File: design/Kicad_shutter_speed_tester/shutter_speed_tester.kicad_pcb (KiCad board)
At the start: 2 copper layers, 17 parts, among them J1 Light Sensor, J2 Light source LED, J3 LCD, J4 Power, Q1 PN2222A, SW1 Reset switch

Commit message: adding routing
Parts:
- moved H4 2.84 mm to (213.4, 129.5)
- moved H3 2.84 mm to (170.2, 129.5)
- moved H2 2.54 mm to (213.4, 85.1)
- moved J3 2.54 mm to (172.7, 119.4)
- moved H1 2.54 mm to (170.2, 85.1)
- moved J4 1.27 mm to (179.1, 110.5)
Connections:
- J4 pad 1: Net-(A1-Pad30) -> GND
- J4 pad 2: GND -> Net-(A1-Pad30)
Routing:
- net GND: track 0.00 -> 87.2 mm
- net Net-(A1-Pad5): track 0.00 -> 63.2 mm
- net Net-(J2-Pad1): track 0.00 -> 57.3 mm
- net Net-(A1-Pad27): track 0.00 -> 52.0 mm
- net Net-(A1-Pad7): track 0.00 -> 43.0 mm
- net Net-(A1-Pad30): track 0.00 -> 31.6 mm
- net Net-(D1-Pad1): track 0.00 -> 29.1 mm
- net Net-(Q1-Pad2): track 0.00 -> 22.6 mm
- net Net-(A1-Pad6): track 0.00 -> 19.1 mm
- net Net-(A1-Pad23): track 0.00 -> 14.6 mm
- net Net-(A1-Pad8): track 0.00 -> 12.5 mm
- net Net-(Q1-Pad3): track 0.00 -> 12.0 mm
- net Net-(A1-Pad24): track 0.00 -> 11.0 mm
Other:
- board outline added: 50.8 x 52.1 mm
- board text added: "LCD"
- board text added: "Light Sensor"
- board text added: "Light Source"
- board text added: "Power"

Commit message: pcb design described
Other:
- board text added: "+"
- board text added: "+5V"
- board text added: "-"
- board text added: "Gnd"
- board text added: "SCL"
- board text added: "SDA"
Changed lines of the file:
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@@
   (general
     (thickness 1.6)
-    (drawings 8)
+    (drawings 22)
     (tracks 77)
     (zones 0)
@@
     )
   )
+  (gr_text SCL (at 180.34 124.46 90) (layer F.SilkS)
+    (effects (font (size 1 1) (thickness 0.15)))
+  )
+  (gr_text SDA (at 177.8 124.46 90) (layer F.SilkS)
+    (effects (font (size 1 1) (thickness 0.15)))
+  )
+  (gr_text +5V (at 175.26 124.46 90) (layer F.SilkS)
+    (effects (font (size 1 1) (thickness 0.15)))
+  )
+  (gr_text Gnd (at 172.72 124.46 90) (layer F.SilkS)
+    (effects (font (size 1 1) (thickness 0.15)))
+  )
+  (gr_text + (at 176.53 114.3) (layer F.SilkS)
+    (effects (font (size 1 1) (thickness 0.15)))
+  )
+  (gr_text - (at 179.07 114.3) (layer F.SilkS)
+    (effects (font (size 1 1) (thickness 0.15)))
+  )
+  (gr_text - (at 179.07 105.41) (layer F.SilkS)
+    (effects (font (size 1 1) (thickness 0.15)))
+  )
+  (gr_text + (at 176.53 105.41) (layer F.SilkS)
+    (effects (font (size 1 1) (thickness 0.15)))
+  )
+  (gr_text - (at 179.07 96.52) (layer F.SilkS)
+    (effects (font (size 1 1) (thickness 0.15)))
+  )
+  (gr_text + (at 176.53 96.52) (layer F.SilkS)
+    (effects (font (size 1 1) (thickness 0.15)))
+  )
+  (gr_line (start 196.85 83.82) (end 189.23 83.82) (layer F.SilkS) (width 0.12))
+  (gr_line (start 196.85 93.98) (end 196.85 83.82) (layer F.SilkS) (width 0.12))
+  (gr_line (start 189.23 93.98) (end 196.85 93.98) (layer F.SilkS) (width 0.12))
+  (gr_line (start 189.23 83.82) (end 189.23 93.98) (layer F.SilkS) (width 0.12))
   (gr_line (start 217.17 81.28) (end 217.17 133.35) (layer Edge.Cuts) (width 0.1))
   (gr_line (start 166.37 81.28) (end 217.17 81.28) (layer Edge.Cuts) (width 0.1))

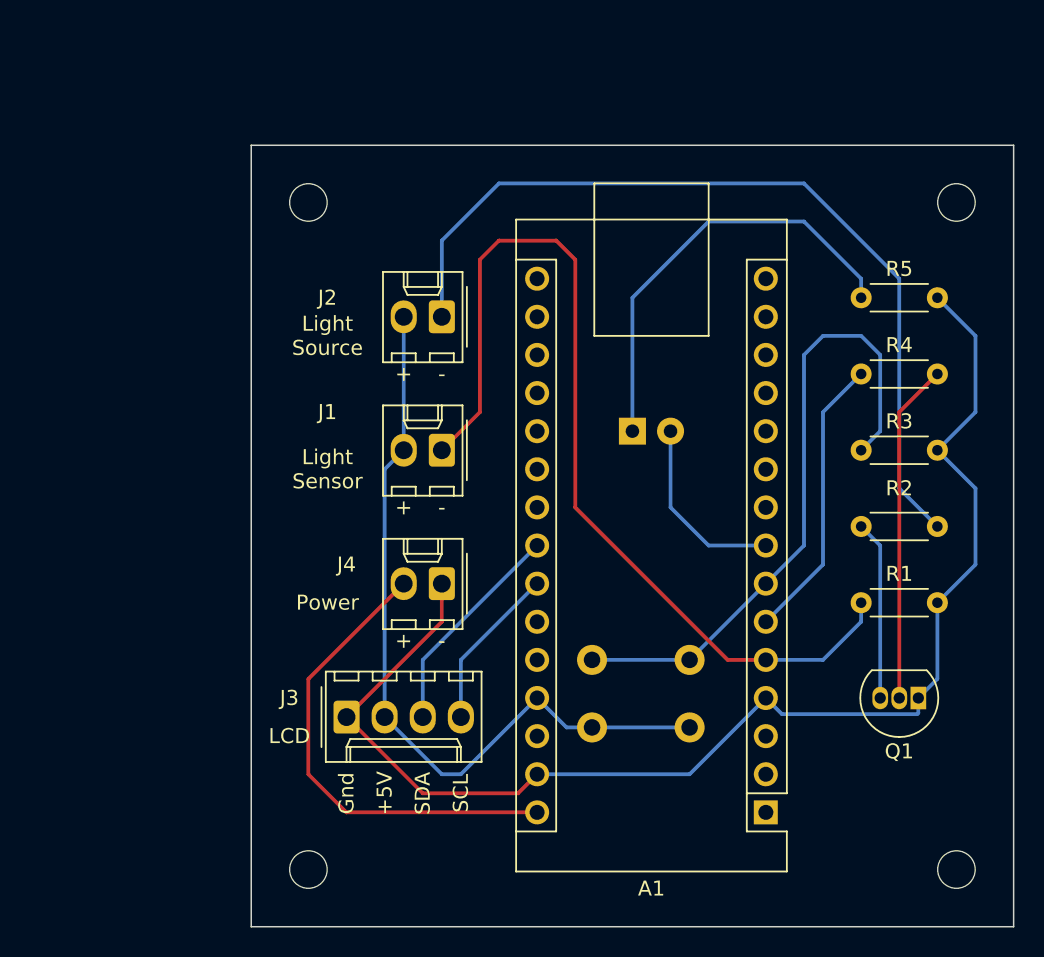
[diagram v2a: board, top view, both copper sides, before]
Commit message: reorganize pcb with USB port on top
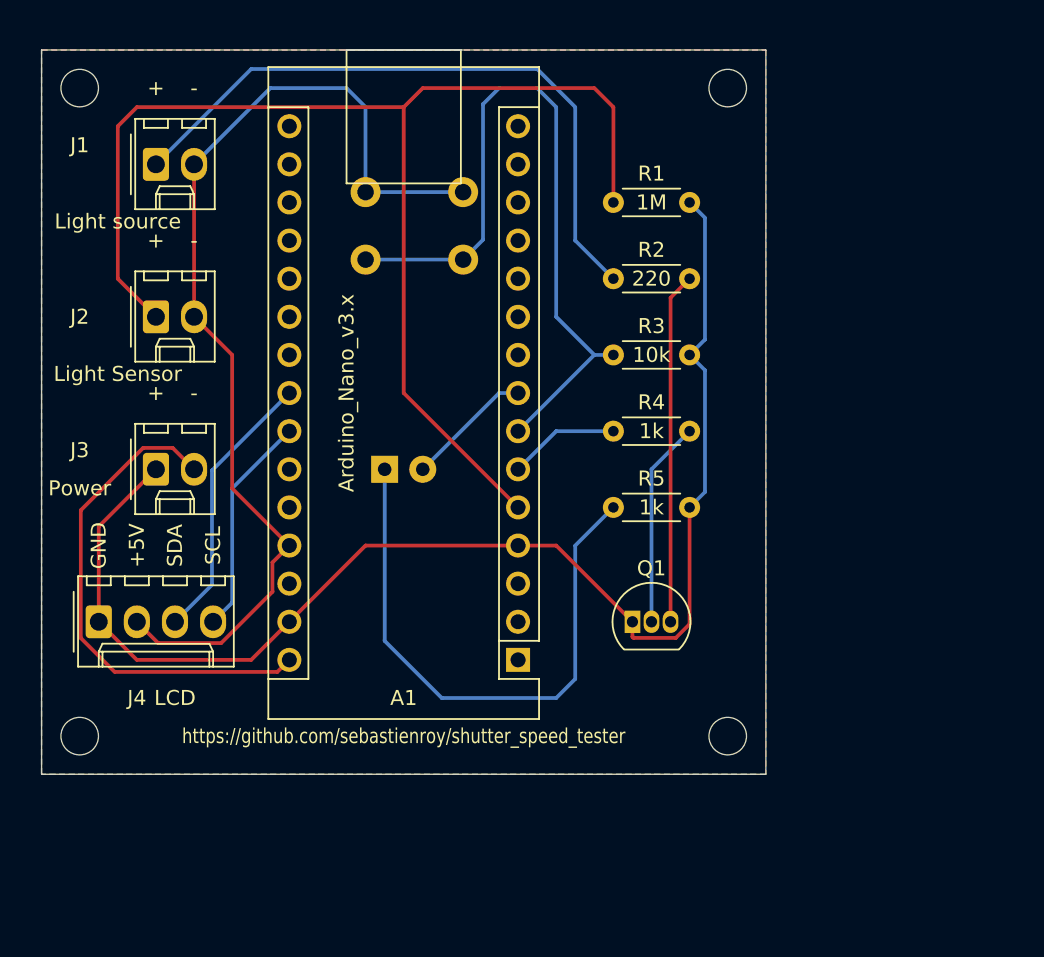
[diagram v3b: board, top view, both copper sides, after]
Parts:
- J1: value Light Sensor -> Light source
- J2: value Light source LED -> Light Sensor
- J3: value LCD -> Power; footprint Connector_Molex:Molex_KK-254_AE-6410-04A_1x04_P2.54mm_Vertical -> Connector_Molex:Molex_KK-254_AE-6410-02A_1x02_P2.54mm_Vertical
- J4: value Power -> LCD; footprint Connector_Molex:Molex_KK-254_AE-6410-02A_1x02_P2.54mm_Vertical -> Connector_Molex:Molex_KK-254_AE-6410-04A_1x04_P2.54mm_Vertical
- moved SW1 34.3 mm to (174.0, 88.9), turned to 0 degrees
- moved R1 31.4 mm to (190.5, 85.1)
- moved R2 27.2 mm to (190.5, 90.2), turned to 0 degrees
- moved J1 26.9 mm to (160.0, 82.5), turned to 0 degrees
- moved J4 23.0 mm to (156.2, 113.0), turned to 0 degrees
- moved R5 21.6 mm to (190.5, 105.4)
- moved J3 20.8 mm to (160.0, 102.9)
- moved Q1 19.7 mm to (191.8, 113.0), turned to 0 degrees
- moved A1 19.4 mm to (184.2, 115.6)
- moved J2 19.0 mm to (160.0, 92.7), turned to 0 degrees
- moved R3 17.7 mm to (190.5, 95.2)
- moved H3 17.6 mm to (154.9, 120.7)
- moved H4 17.6 mm to (198.1, 120.7)
- moved H1 17.0 mm to (154.9, 77.5)
- moved H2 17.0 mm to (198.1, 77.5)
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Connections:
- J1 pad 1: Net-(A1-Pad5) -> Net-(J1-Pad1)
- J2 pad 1: Net-(J2-Pad1) -> Net-(A1-Pad5)
- J3 pad 2: Net-(A1-Pad27) -> Net-(A1-Pad30)
- J4 pad 2: Net-(A1-Pad30) -> Net-(A1-Pad27)
- R2 pad 1: Net-(J2-Pad1) -> Net-(J1-Pad1)
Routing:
- net Net-(J2-Pad1): track 57.3 -> 0.00 mm
- net Net-(J1-Pad1): track 0.00 -> 44.1 mm
- net Net-(A1-Pad5): track 63.2 -> 84.5 mm
- net Net-(A1-Pad27): track 52.0 -> 68.8 mm
- net Net-(A1-Pad6): track 19.1 -> 7.40 mm
- net Net-(Q1-Pad3): track 12.0 -> 23.4 mm
- net Net-(D1-Pad1): track 29.1 -> 38.7 mm
- net Net-(Q1-Pad2): track 22.6 -> 13.8 mm
- net Net-(A1-Pad7): track 43.0 -> 49.3 mm
- net Net-(A1-Pad8): track 12.5 -> 8.45 mm
- net Net-(A1-Pad23): track 14.6 -> 18.4 mm
- net Net-(A1-Pad24): track 11.0 -> 14.8 mm
- net Net-(A1-Pad30): track 31.6 -> 33.5 mm
- net GND: track 87.2 -> 88.6 mm
- added copper zone on B.Cu, net GND
- added copper zone on F.Cu, net GND
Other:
- board size 50.8 x 52.1 mm -> 48.3 x 48.3 mm
- board text added: "GND"
- board text added: "https://github.com/sebastienroy/shutter_speed_tester"
- board text removed: "Gnd"
- board text removed: "LCD"
- board text removed: "Light Sensor"
- board text removed: "Light Source"
- board text removed: "Power"

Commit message: move components
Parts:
- moved SW1 3.81 mm to (174.0, 92.7)
- moved D1 2.54 mm to (175.3, 105.4)
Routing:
- net Net-(A1-Pad7): track 49.3 -> 53.1 mm
- net Net-(A1-Pad27): track 68.8 -> 72.6 mm
- net Net-(D1-Pad1): track 38.7 -> 36.2 mm
- net Net-(A1-Pad8): track 8.45 -> 10.3 mm
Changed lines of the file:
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@@
     (thickness 1.6)
     (drawings 19)
-    (tracks 86)
+    (tracks 87)
     (zones 0)
     (modules 17)
@@
   )
   (module Button_Switch_THT:SW_PUSH_6mm_H5mm (layer B.Cu)
-    (at 173.99 88.9)
+    (at 173.99 92.71)
     (descr "tactile push button, 6x6mm e.g. PHAP33xx series, height=5mm")
     (tags "tact sw push 6mm")
@@
   )
   (module LED_THT:LED_D3.0mm (layer B.Cu)
-    (at 175.26 102.87)
+    (at 175.26 105.41)
     (descr "LED, diameter 3.0mm, 2 pins")
     (tags "LED diameter 3.0mm 2 pins")
@@
   (segment (start 165.1 111.76) (end 165.1 104.14) (width 0.25) (layer B.Cu) (net 1))
   (segment (start 163.83 113.03) (end 165.1 111.76) (width 0.25) (layer B.Cu) (net 1))
-  (segment (start 182.88 97.79) (end 184.15 97.79) (width 0.25) (layer B.Cu) (net 2))
-  (segment (start 177.8 102.87) (end 182.88 97.79) (width 0.25) (layer B.Cu) (net 2))
+  (segment (start 177.8 104.14) (end 177.8 105.41) (width 0.25) (layer B.Cu) (net 2))
+  (segment (start 184.15 97.79) (end 177.8 104.14) (width 0.25) (layer B.Cu) (net 2))
   (segment (start 163.75501 102.94499) (end 168.91 97.79) (width 0.25) (layer B.Cu) (net 3))
   (segment (start 163.75501 110.56499) (end 163.75501 102.94499) (width 0.25) (layer B.Cu) (net 3))
   (segment (start 161.29 113.03) (end 163.75501 110.56499) (width 0.25) (layer B.Cu) (net 3))
-  (segment (start 173.99 88.9) (end 180.49 88.9) (width 0.25) (layer B.Cu) (net 4))
-  (segment (start 186.69 92.71) (end 189.23 95.25) (width 0.25) (layer B.Cu) (net 4))
-  (segment (start 185.42 77.47) (end 186.69 78.74) (width 0.25) (layer B.Cu) (net 4))
-  (segment (start 182.88 77.47) (end 185.42 77.47) (width 0.25) (layer B.Cu) (net 4))
-  (segment (start 181.815001 78.534999) (end 182.88 77.47) (width 0.25) (layer B.Cu) (net 4))
-  (segment (start 186.69 78.74) (end 186.69 92.71) (width 0.25) (layer B.Cu) (net 4))
-  (segment (start 181.815001 87.574999) (end 181.815001 78.534999) (width 0.25) (layer B.Cu) (net 4))
-  (segment (start 180.49 88.9) (end 181.815001 87.574999) (width 0.25) (layer B.Cu) (net 4))
   (segment (start 189.23 95.25) (end 184.15 100.33) (width 0.25) (layer B.Cu) (net 4))
   (segment (start 190.5 95.25) (end 189.23 95.25) (width 0.25) (layer B.Cu) (net 4))
+  (segment (start 181.815001 91.384999) (end 180.49 92.71) (width 0.25) (layer B.Cu) (net 4))
+  (segment (start 182.88 77.47) (end 181.815001 78.534999) (width 0.25) (layer B.Cu) (net 4))
+  (segment (start 185.42 77.47) (end 182.88 77.47) (width 0.25) (layer B.Cu) (net 4))
+  (segment (start 186.69 78.74) (end 185.42 77.47) (width 0.25) (layer B.Cu) (net 4))
+  (segment (start 186.69 92.71) (end 186.69 78.74) (width 0.25) (layer B.Cu) (net 4))
+  (segment (start 181.815001 78.534999) (end 181.815001 91.384999) (width 0.25) (layer B.Cu) (net 4))
+  (segment (start 189.23 95.25) (end 186.69 92.71) (width 0.25) (layer B.Cu) (net 4))
+  (segment (start 173.99 92.71) (end 180.49 92.71) (width 0.25) (layer B.Cu) (net 4))
   (segment (start 186.69 100.33) (end 184.15 102.87) (width 0.25) (layer B.Cu) (net 5))
   (segment (start 190.5 100.33) (end 186.69 100.33) (width 0.25) (layer B.Cu) (net 5))
@@
   (segment (start 173.99 78.74) (end 173.99 84.4) (width 0.25) (layer B.Cu) (net 9))
   (segment (start 172.72 77.47) (end 173.99 78.74) (width 0.25) (layer B.Cu) (net 9))
-  (segment (start 173.99 84.4) (end 180.49 84.4) (width 0.25) (layer B.Cu) (net 9))
-  (segment (start 175.26 114.3) (end 175.26 102.87) (width 0.25) (layer B.Cu) (net 10))
+  (segment (start 173.99 84.4) (end 173.99 88.21) (width 0.25) (layer B.Cu) (net 9))
+  (segment (start 173.99 88.21) (end 180.49 88.21) (width 0.25) (layer B.Cu) (net 9))
   (segment (start 179.07 118.11) (end 175.26 114.3) (width 0.25) (layer B.Cu) (net 10))
   (segment (start 186.69 118.11) (end 179.07 118.11) (width 0.25) (layer B.Cu) (net 10))
@@
   (segment (start 187.96 116.84) (end 186.69 118.11) (width 0.25) (layer B.Cu) (net 10))
   (segment (start 190.5 105.41) (end 187.96 107.95) (width 0.25) (layer B.Cu) (net 10))
+  (segment (start 175.26 114.3) (end 175.26 105.41) (width 0.25) (layer B.Cu) (net 10))
   (segment (start 194.31 91.44) (end 194.31 113.03) (width 0.25) (layer F.Cu) (net 11))
   (segment (start 195.58 90.17) (end 194.31 91.44) (width 0.25) (layer F.Cu) (net 11))

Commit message: update board
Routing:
- net GND: track 88.6 -> 96.8 mm
- net Net-(A1-Pad5): track 84.5 -> 78.4 mm

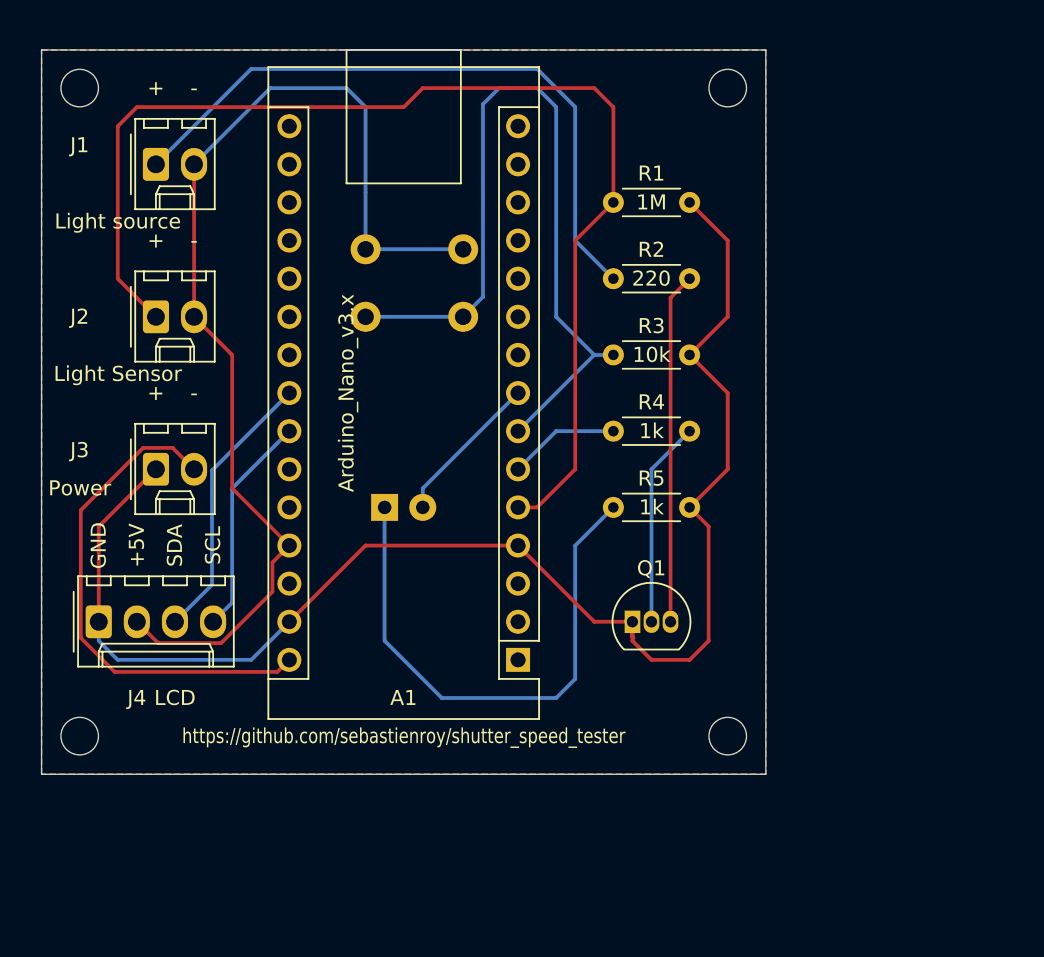
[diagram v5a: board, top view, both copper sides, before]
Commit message: Changes on PCB, fixes #2, fixes #3, fixes #4
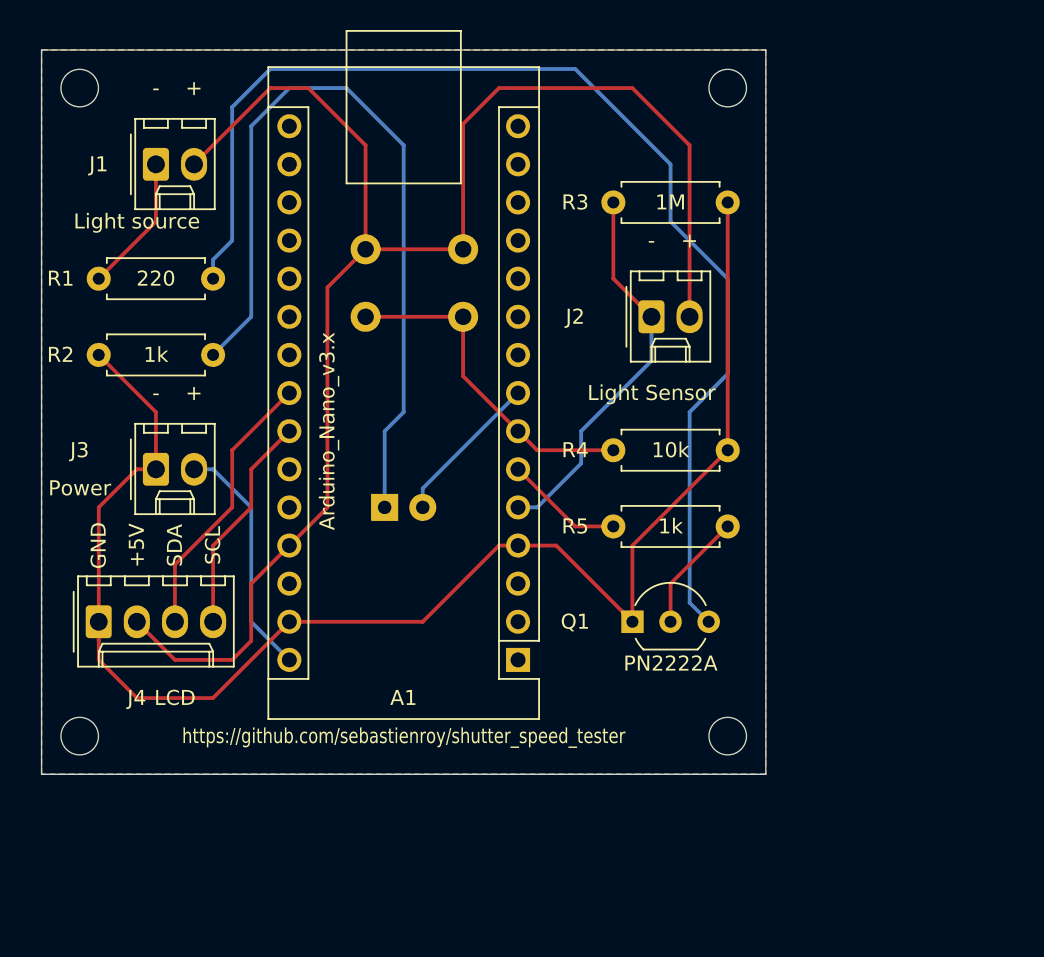
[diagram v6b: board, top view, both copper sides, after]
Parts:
- Q1: footprint Package_TO_SOT_THT:TO-92_Inline -> Package_TO_SOT_THT:TO-92_Inline_Wide
- R1: renamed from R2; footprint Resistor_THT:R_Axial_DIN0204_L3.6mm_D1.6mm_P5.08mm_Horizontal -> Resistor_THT:R_Axial_DIN0207_L6.3mm_D2.5mm_P7.62mm_Horizontal
- R2: renamed from R5; footprint Resistor_THT:R_Axial_DIN0204_L3.6mm_D1.6mm_P5.08mm_Horizontal -> Resistor_THT:R_Axial_DIN0207_L6.3mm_D2.5mm_P7.62mm_Horizontal
- R3: renamed from R1; footprint Resistor_THT:R_Axial_DIN0204_L3.6mm_D1.6mm_P5.08mm_Horizontal -> Resistor_THT:R_Axial_DIN0207_L6.3mm_D2.5mm_P7.62mm_Horizontal
- R4: renamed from R3; footprint Resistor_THT:R_Axial_DIN0204_L3.6mm_D1.6mm_P5.08mm_Horizontal -> Resistor_THT:R_Axial_DIN0207_L6.3mm_D2.5mm_P7.62mm_Horizontal
- R5: renamed from R4; footprint Resistor_THT:R_Axial_DIN0204_L3.6mm_D1.6mm_P5.08mm_Horizontal -> Resistor_THT:R_Axial_DIN0207_L6.3mm_D2.5mm_P7.62mm_Horizontal
- moved R1 34.3 mm to (156.2, 90.2)
- moved J2 33.0 mm to (193.0, 92.7)
- moved R2 28.5 mm to (163.8, 95.2), turned to 180 degrees
- moved R5 6.35 mm to (190.5, 106.7)
- moved R4 6.35 mm to (190.5, 101.6)
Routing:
- net Net-(Q1-Pad3): track 23.4 -> 78.5 mm
- net Net-(A1-Pad5): track 78.4 -> 25.8 mm
- net Net-(J1-Pad1): track 44.1 -> 9.20 mm
- net Net-(A1-Pad27): track 72.6 -> 104.4 mm
- net Net-(A1-Pad7): track 53.1 -> 22.5 mm
- net Net-(D1-Pad1): track 36.2 -> 53.7 mm
- net Net-(A1-Pad30): track 33.5 -> 16.1 mm
- net Net-(Q1-Pad2): track 13.8 -> 7.93 mm
- net GND: track 96.8 -> 99.0 mm
- net Net-(A1-Pad6): track 7.40 -> 7.93 mm

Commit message: Casing...
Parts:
- D1: footprint LED_THT:LED_D3.0mm -> LED_THT:LED_D5.0mm
